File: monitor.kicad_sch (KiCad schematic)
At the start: 4 parts, among them U1 PAT1220-C-6DB, U2 HMC525ALC4

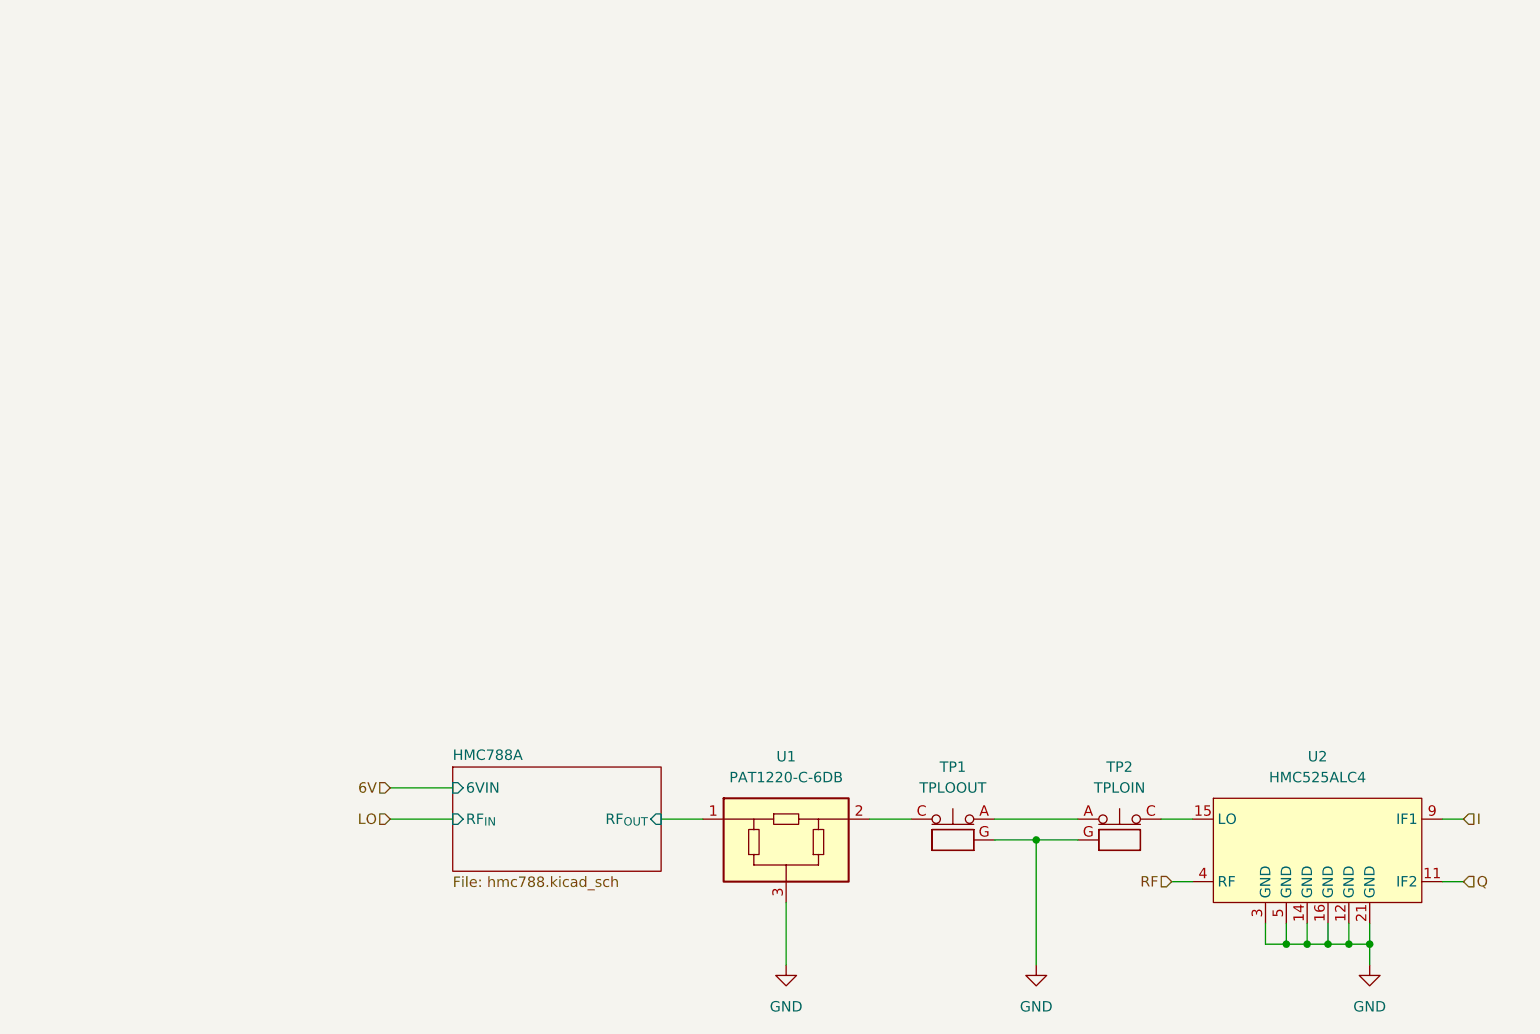
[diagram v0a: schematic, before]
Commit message: Add Clock sources and monitor output
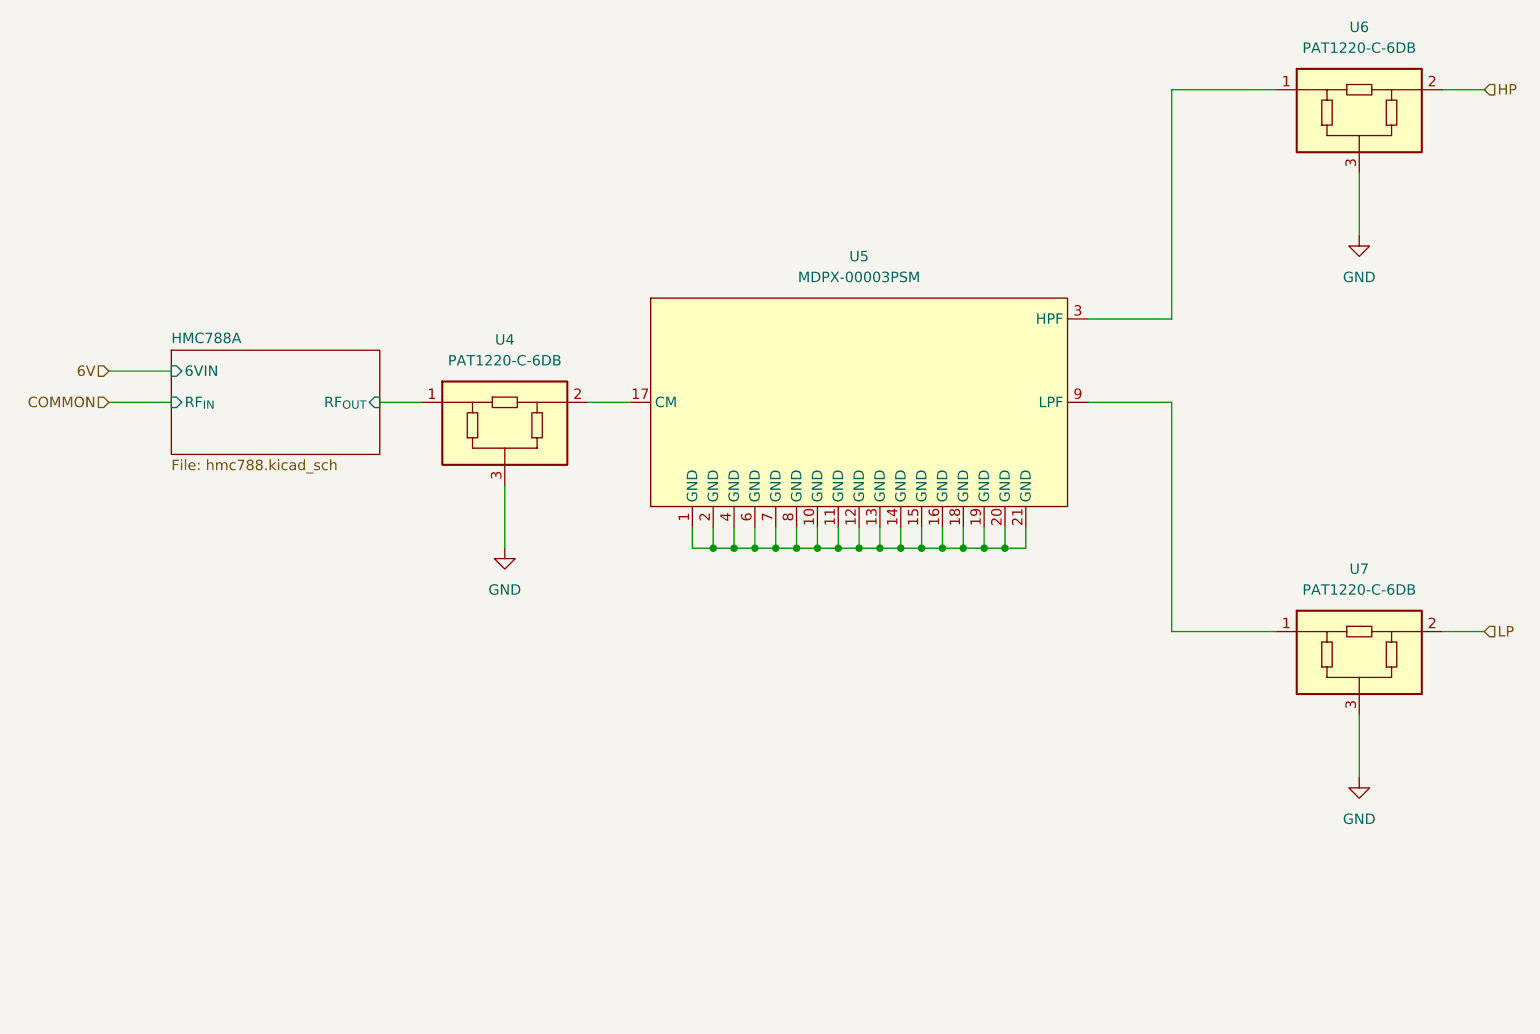
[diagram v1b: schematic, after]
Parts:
- removed TP1: TPLOOUT, Connector_Coaxial:CoaxialSwitch_Hirose_MS-156C3_Horizontal, symbol Connector:CoaxialSwitch_Testpoint
- removed TP2: TPLOIN, Connector_Coaxial:CoaxialSwitch_Hirose_MS-156C3_Horizontal, symbol Connector:CoaxialSwitch_Testpoint
- removed U1: PAT1220-C-6DB, RF_Converter:RF_Attenuator_Susumu_PAT1220, symbol RF:PAT1220-C-6DB
- removed U2: HMC525ALC4, Package_DFN_QFN:QFN-24-1EP_4x4mm_P0.5mm_EP2.7x2.7mm_ThermalVias, symbol huskylib:HMC525ALC4
- added U4, U6, U7: PAT1220-C-6DB, RF_Converter:RF_Attenuator_Susumu_PAT1220, symbol RF:PAT1220-C-6DB
- added U5: MDPX-00003PSM, symbol huskylib:MDPX-00003PSM
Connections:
- net GND: now also U4.3, U6.3, U7.3
- net HMC788A/RF_{OUT}: now also U4.1
- new net: U5.3 (HPF), U6.1
- new net: U5.9 (LPF), U7.1
- new net: U4.2, U5.17 (CM)
- new net: U5.1 (GND), U5.10 (GND), U5.11 (GND), U5.12 (GND), U5.13 (GND), U5.14 (GND), U5.15 (GND), U5.16 (GND), U5.18 (GND), U5.19 (GND), U5.2 (GND), U5.20 (GND), U5.21 (GND), U5.4 (GND), U5.6 (GND), U5.7 (GND), U5.8 (GND)
- new net HP: U6.2
- new net LP: U7.2

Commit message: Round 1 review comments
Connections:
- net GND: now also U5.1 (GND), U5.10 (GND), U5.11 (GND), U5.12 (GND), U5.13 (GND), U5.14 (GND), U5.15 (GND), U5.16 (GND), U5.18 (GND), U5.19 (GND), U5.2 (GND), U5.20 (GND), U5.21 (GND), U5.4 (GND), U5.6 (GND), U5.7 (GND), U5.8 (GND)
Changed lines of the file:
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@@
+	(wire
+		(pts
+			(xy 127 132.08) (xy 127 134.62)
+		)
+		(stroke
+			(width 0)
+			(type default)
+		)
+	)
 	(wire
 		(pts
@@
 		(dnp no)
 		(fields_autoplaced yes)
-		(property "Reference" "#PWR016"
+		(property "Reference" "#PWR019"
 			(at 83.82 138.43 0)
 			(hide yes)
@@
 			(project "huskypointofload"
 				(path "/eb9c972b-d134-41da-be97-ece3f463f7e0/cb2bed6b-53a5-4f58-b70f-ffa107cbb07d"
-					(reference "#PWR016")
+					(reference "#PWR019")
 					(unit 1)
 				)
@@
 		(dnp no)
 		(fields_autoplaced yes)
-		(property "Reference" "#PWR017"
+		(property "Reference" "#PWR020"
 			(at 187.96 100.33 0)
 			(hide yes)
@@
 			(project "huskypointofload"
 				(path "/eb9c972b-d134-41da-be97-ece3f463f7e0/cb2bed6b-53a5-4f58-b70f-ffa107cbb07d"
-					(reference "#PWR017")
+					(reference "#PWR020")
+					(unit 1)
+				)
+			)
+		)
+	)
+	(symbol
+		(lib_id "power:GND")
+		(at 127 134.62 0)
+		(unit 1)
+		(body_style 1)
+		(exclude_from_sim no)
+		(in_bom yes)
+		(on_board yes)
+		(in_pos_files yes)
+		(dnp no)
+		(fields_autoplaced yes)
+		(property "Reference" "#PWR0319"
+			(at 127 140.97 0)
+			(hide yes)
+			(show_name no)
+			(do_not_autoplace no)
+			(effects
+				(font
+					(size 1.27 1.27)
+				)
+			)
+		)
+		(property "Value" "GND"
+			(at 127 139.7 0)
+			(show_name no)
+			(do_not_autoplace no)
+			(effects
+				(font
+					(size 1.27 1.27)
+				)
+			)
+		)
+		(property "Footprint" ""
+			(at 127 134.62 0)
+			(hide yes)
+			(show_name no)
+			(do_not_autoplace no)
+			(effects
+				(font
+					(size 1.27 1.27)
+				)
+			)
+		)
+		(property "Datasheet" ""
+			(at 127 134.62 0)
+			(hide yes)
+			(show_name no)
+			(do_not_autoplace no)
+			(effects
+				(font
+					(size 1.27 1.27)
+				)
+			)
+		)
+		(property "Description" "Power symbol creates a global label with name \"GND\" , ground"
+			(at 127 134.62 0)
+			(hide yes)
+			(show_name no)
+			(do_not_autoplace no)
+			(effects
+				(font
+					(size 1.27 1.27)
+				)
+			)
+		)
+		(pin "1"
+		)
+		(instances
+			(project "huskypointofload"
+				(path "/eb9c972b-d134-41da-be97-ece3f463f7e0/cb2bed6b-53a5-4f58-b70f-ffa107cbb07d"
+					(reference "#PWR0319")
 					(unit 1)
 				)
@@
 		(dnp no)
 		(fields_autoplaced yes)
-		(property "Reference" "#PWR018"
+		(property "Reference" "#PWR021"
 			(at 187.96 166.37 0)
 			(hide yes)
@@
 			(project "huskypointofload"
 				(path "/eb9c972b-d134-41da-be97-ece3f463f7e0/cb2bed6b-53a5-4f58-b70f-ffa107cbb07d"
-					(reference "#PWR018")
+					(reference "#PWR021")
 					(unit 1)
 				)

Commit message: Round 2 Review, power tree cleanup
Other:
- sheet HMC788A ports: added 5VIN; removed 6VIN
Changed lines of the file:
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@@
 		)
 	)
-	(hierarchical_label "6V"
+	(hierarchical_label "5V"
 		(shape input)
 		(at 35.56 110.49 180)
@@
 		(dnp no)
 		(fields_autoplaced yes)
-		(property "Reference" "#PWR019"
+		(property "Reference" "#PWR022"
 			(at 83.82 138.43 0)
 			(hide yes)
@@
 			(project "huskypointofload"
 				(path "/eb9c972b-d134-41da-be97-ece3f463f7e0/cb2bed6b-53a5-4f58-b70f-ffa107cbb07d"
-					(reference "#PWR019")
+					(reference "#PWR022")
 					(unit 1)
 				)
@@
 		(dnp no)
 		(fields_autoplaced yes)
-		(property "Reference" "#PWR020"
+		(property "Reference" "#PWR024"
 			(at 187.96 100.33 0)
 			(hide yes)
@@
 			(project "huskypointofload"
 				(path "/eb9c972b-d134-41da-be97-ece3f463f7e0/cb2bed6b-53a5-4f58-b70f-ffa107cbb07d"
-					(reference "#PWR020")
+					(reference "#PWR024")
 					(unit 1)
 				)
@@
 		(dnp no)
 		(fields_autoplaced yes)
-		(property "Reference" "#PWR0319"
+		(property "Reference" "#PWR023"
 			(at 127 140.97 0)
 			(hide yes)
@@
 			(project "huskypointofload"
 				(path "/eb9c972b-d134-41da-be97-ece3f463f7e0/cb2bed6b-53a5-4f58-b70f-ffa107cbb07d"
-					(reference "#PWR0319")
+					(reference "#PWR023")
 					(unit 1)
 				)
@@
 		(dnp no)
 		(fields_autoplaced yes)
-		(property "Reference" "#PWR021"
+		(property "Reference" "#PWR025"
 			(at 187.96 166.37 0)
 			(hide yes)
@@
 			(project "huskypointofload"
 				(path "/eb9c972b-d134-41da-be97-ece3f463f7e0/cb2bed6b-53a5-4f58-b70f-ffa107cbb07d"
-					(reference "#PWR021")
+					(reference "#PWR025")
 					(unit 1)
 				)
@@
 			)
 		)
-		(pin "6VIN" input
-			(at 43.18 110.49 180)
-			(effects
-				(font
-					(size 1.27 1.27)
-				)
-				(justify left)
-			)
-		)
 		(pin "RF_{IN}" input
 			(at 43.18 114.3 180)
@@
 			)
 		)
+		(pin "5VIN" input
+			(at 43.18 110.49 180)
+			(effects
+				(font
+					(size 1.27 1.27)
+				)
+				(justify left)
+			)
+		)
